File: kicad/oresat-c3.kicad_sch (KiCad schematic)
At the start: 0 parts

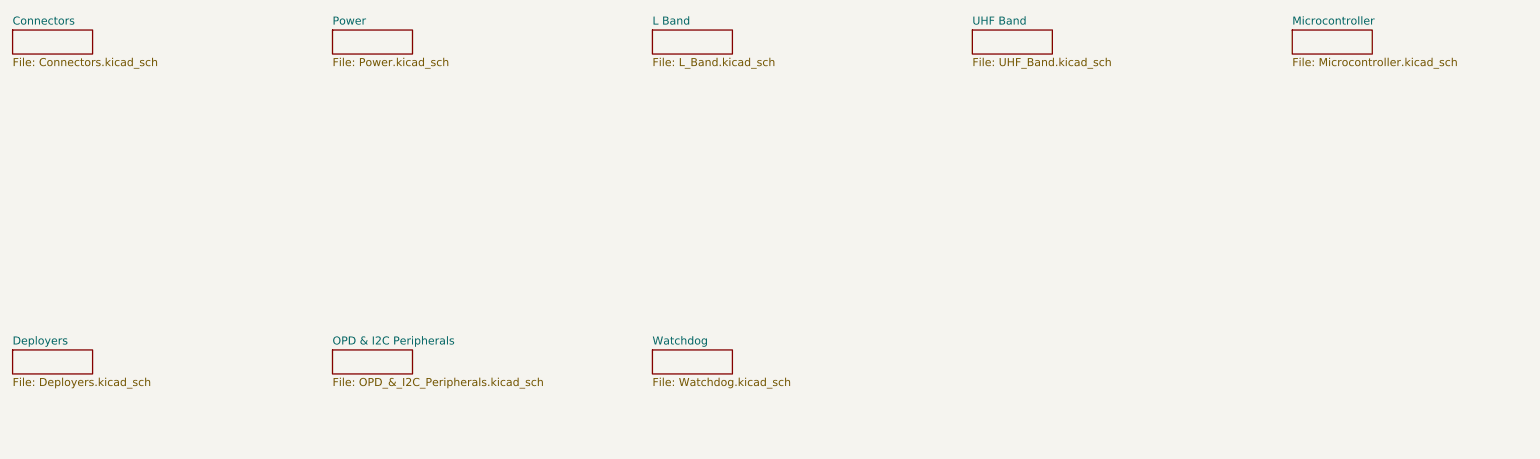
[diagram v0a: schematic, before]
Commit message: Converted kicad directory over to our latest Octavo-based v6 design starting from the GPS card.
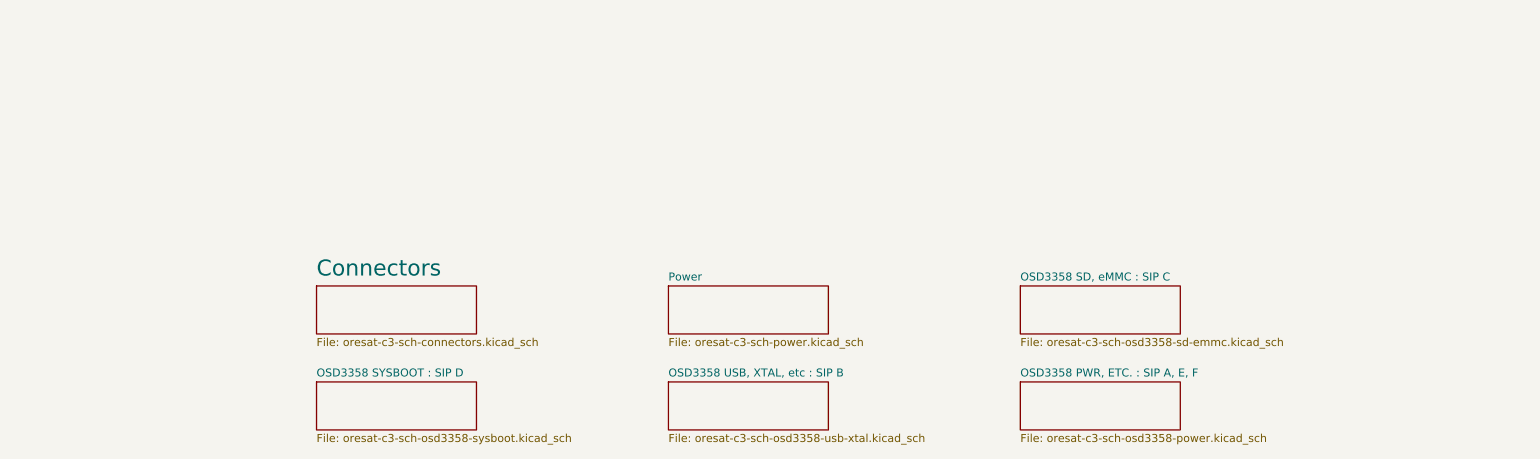
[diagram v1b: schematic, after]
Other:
- removed sheet Deployers
- removed sheet L Band
- removed sheet Microcontroller
- removed sheet OPD & I2C Peripherals
- removed sheet UHF Band
- removed sheet Watchdog
- added sheet OSD3358 PWR, ETC. : SIP A, E, F (oresat-c3-sch-osd3358-power.kicad_sch)
- added sheet OSD3358 SD, eMMC : SIP C (oresat-c3-sch-osd3358-sd-emmc.kicad_sch)
- added sheet OSD3358 SYSBOOT : SIP D (oresat-c3-sch-osd3358-sysboot.kicad_sch)
- added sheet OSD3358 USB, XTAL, etc : SIP B (oresat-c3-sch-osd3358-usb-xtal.kicad_sch)
- sheet Connectors: file Connectors.kicad_sch -> oresat-c3-sch-connectors.kicad_sch
- sheet Power: file Power.kicad_sch -> oresat-c3-sch-power.kicad_sch

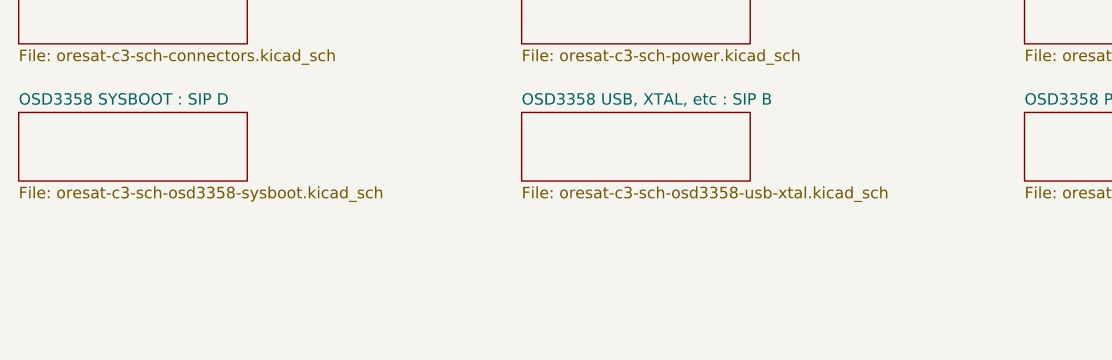
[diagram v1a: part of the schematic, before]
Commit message: Started moving RF schematic bits over to KiCad
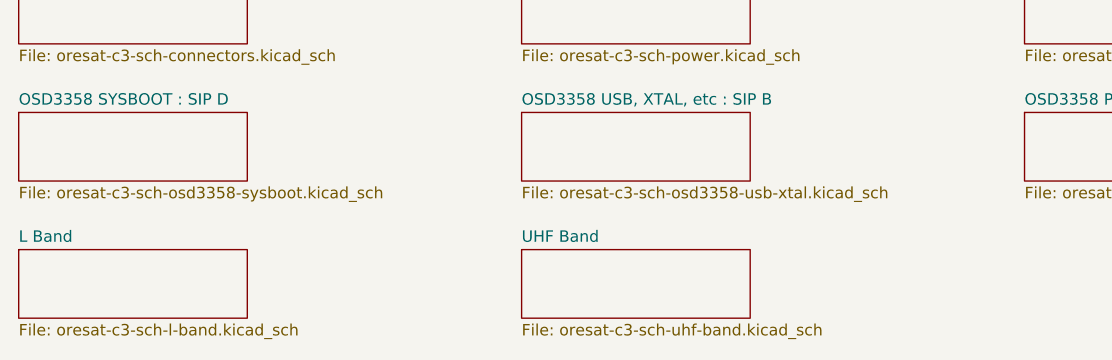
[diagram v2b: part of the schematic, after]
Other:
- added sheet L Band (oresat-c3-sch-l-band.kicad_sch)
- added sheet UHF Band (oresat-c3-sch-uhf-band.kicad_sch)
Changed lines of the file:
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@@
 (kicad_sch (version 20230121) (generator eeschema)
-  (paper "B")
+  (paper "USLedger")
+  (sheet (at 129.54 96.52) (size 25.4 7.62) (fields_autoplaced)
+    (stroke (width 0.1524) (type solid))
+    (fill (color 0 0 0 0.0000))
+    (property "Sheetname" "UHF Band" (at 129.54 95.8084 0)
+      (effects (font (size 1.27 1.27)) (justify left bottom))
+    )
+    (property "Sheetfile" "oresat-c3-sch-uhf-band.kicad_sch" (at 129.54 104.7246 0)
+      (effects (font (size 1.27 1.27)) (justify left top))
+    )
+    (instances
+      (project "oresat-c3"
+        (path "/65d12cdd-c326-4033-9053-c59fa4e0b25e" (page "9"))
+      )
+    )
+  )
   (sheet (at 185.42 81.28) (size 25.4 7.62) (fields_autoplaced)
     (stroke (width 0.1524) (type solid))
@@
       )
     )
+  )
+  (sheet (at 73.66 96.52) (size 25.4 7.62) (fields_autoplaced)
+    (stroke (width 0.1524) (type solid))
+    (fill (color 0 0 0 0.0000))
+    (property "Sheetname" "L Band" (at 73.66 95.8084 0)
+      (effects (font (size 1.27 1.27)) (justify left bottom))
+    )
+    (property "Sheetfile" "oresat-c3-sch-l-band.kicad_sch" (at 73.66 104.7246 0)
+      (effects (font (size 1.27 1.27)) (justify left top))
+    )
+    (instances
+      (project "oresat-c3"
+        (path "/65d12cdd-c326-4033-9053-c59fa4e0b25e" (page "8"))
+      )
+    )

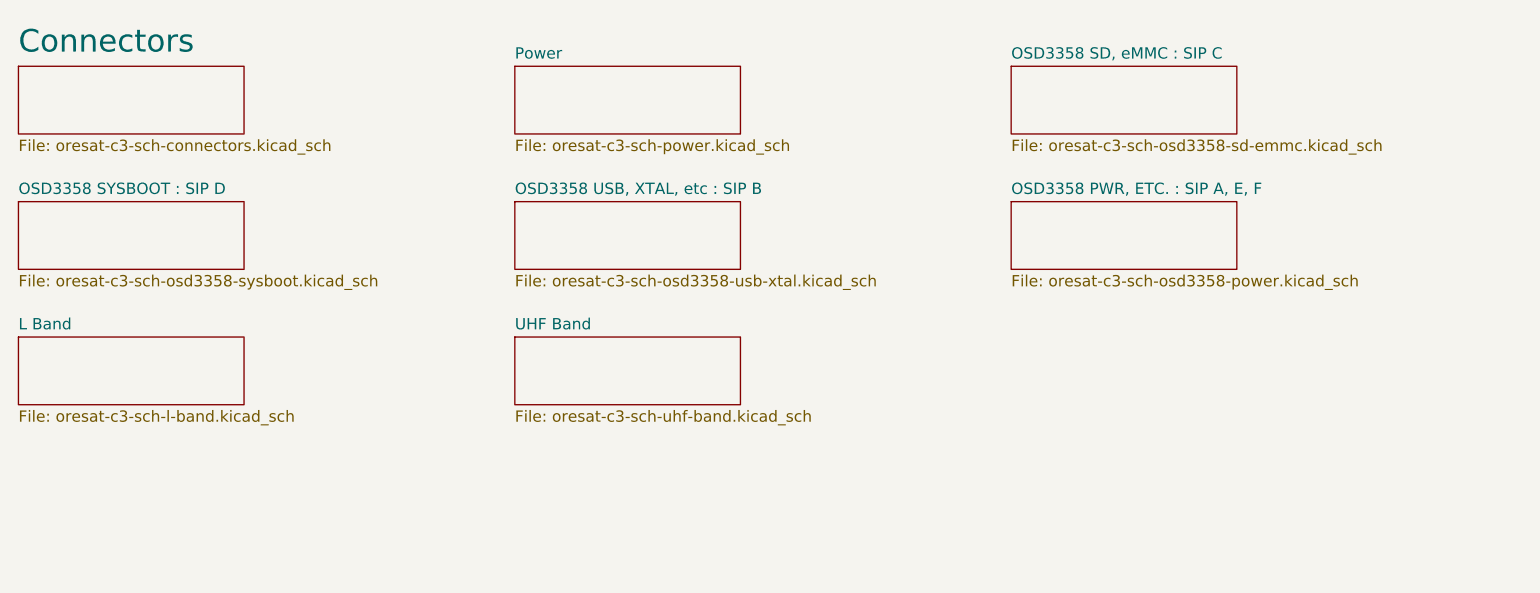
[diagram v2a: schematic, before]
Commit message: Added watchdog and I2C sheets; fixed library paths and library references. Started on watchdog schematic.
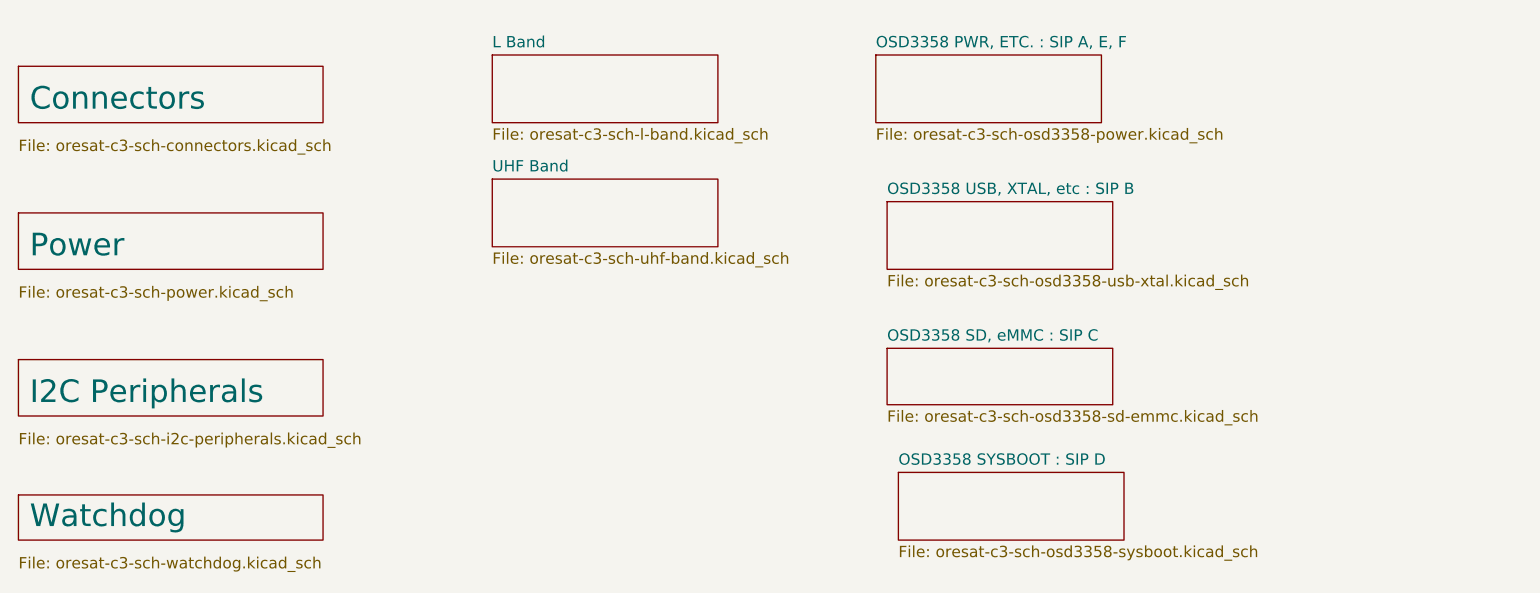
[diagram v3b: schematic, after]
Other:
- added sheet I2C Peripherals (oresat-c3-sch-i2c-peripherals.kicad_sch)
- added sheet Watchdog (oresat-c3-sch-watchdog.kicad_sch)
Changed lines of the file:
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@@
 (kicad_sch (version 20230121) (generator eeschema)
   (paper "USLedger")
-  (sheet (at 129.54 96.52) (size 25.4 7.62) (fields_autoplaced)
+  (sheet (at 127 78.74) (size 25.4 7.62) (fields_autoplaced)
     (stroke (width 0.1524) (type solid))
     (fill (color 0 0 0 0.0000))
-    (property "Sheetname" "UHF Band" (at 129.54 95.8084 0)
+    (property "Sheetname" "UHF Band" (at 127 78.0284 0)
       (effects (font (size 1.27 1.27)) (justify left bottom))
     )
-    (property "Sheetfile" "oresat-c3-sch-uhf-band.kicad_sch" (at 129.54 104.7246 0)
+    (property "Sheetfile" "oresat-c3-sch-uhf-band.kicad_sch" (at 127 86.9446 0)
       (effects (font (size 1.27 1.27)) (justify left top))
     )
@@
     )
   )
-  (sheet (at 185.42 81.28) (size 25.4 7.62) (fields_autoplaced)
+  (sheet (at 170.18 64.77) (size 25.4 7.62) (fields_autoplaced)
     (stroke (width 0.1524) (type solid))
     (fill (color 0 0 0 0.0000))
-    (property "Sheetname" "OSD3358 PWR, ETC. : SIP A, E, F" (at 185.42 80.5684 0)
+    (property "Sheetname" "OSD3358 PWR, ETC. : SIP A, E, F" (at 170.18 64.0584 0)
       (effects (font (size 1.27 1.27)) (justify left bottom))
     )
-    (property "Sheetfile" "oresat-c3-sch-osd3358-power.kicad_sch" (at 185.42 89.4846 0)
+    (property "Sheetfile" "oresat-c3-sch-osd3358-power.kicad_sch" (at 170.18 72.9746 0)
       (effects (font (size 1.27 1.27)) (justify left top))
     )
@@
     )
   )
-  (sheet (at 73.66 81.28) (size 25.4 7.62) (fields_autoplaced)
+  (sheet (at 172.72 111.76) (size 25.4 7.62) (fields_autoplaced)
     (stroke (width 0.1524) (type solid))
     (fill (color 0 0 0 0.0000))
-    (property "Sheetname" "OSD3358 SYSBOOT : SIP D" (at 73.66 80.5684 0)
+    (property "Sheetname" "OSD3358 SYSBOOT : SIP D" (at 172.72 111.0484 0)
       (effects (font (size 1.27 1.27)) (justify left bottom))
     )
-    (property "Sheetfile" "oresat-c3-sch-osd3358-sysboot.kicad_sch" (at 73.66 89.4846 0)
+    (property "Sheetfile" "oresat-c3-sch-osd3358-sysboot.kicad_sch" (at 172.72 119.9646 0)
       (effects (font (size 1.27 1.27)) (justify left top))
     )
@@
     )
   )
-  (sheet (at 129.54 81.28) (size 25.4 7.62) (fields_autoplaced)
+  (sheet (at 171.45 81.28) (size 25.4 7.62) (fields_autoplaced)
     (stroke (width 0.1524) (type solid))
     (fill (color 0 0 0 0.0000))
-    (property "Sheetname" "OSD3358 USB, XTAL, etc : SIP B" (at 129.54 80.5684 0)
+    (property "Sheetname" "OSD3358 USB, XTAL, etc : SIP B" (at 171.45 80.5684 0)
       (effects (font (size 1.27 1.27)) (justify left bottom))
     )
-    (property "Sheetfile" "oresat-c3-sch-osd3358-usb-xtal.kicad_sch" (at 129.54 89.4846 0)
+    (property "Sheetfile" "oresat-c3-sch-osd3358-usb-xtal.kicad_sch" (at 171.45 89.4846 0)
       (effects (font (size 1.27 1.27)) (justify left top))
     )
@@
     )
   )
-  (sheet (at 73.66 96.52) (size 25.4 7.62) (fields_autoplaced)
+  (sheet (at 127 64.77) (size 25.4 7.62) (fields_autoplaced)
     (stroke (width 0.1524) (type solid))
     (fill (color 0 0 0 0.0000))
-    (property "Sheetname" "L Band" (at 73.66 95.8084 0)
+    (property "Sheetname" "L Band" (at 127 64.0584 0)
       (effects (font (size 1.27 1.27)) (justify left bottom))
     )
-    (property "Sheetfile" "oresat-c3-sch-l-band.kicad_sch" (at 73.66 104.7246 0)
+    (property "Sheetfile" "oresat-c3-sch-l-band.kicad_sch" (at 127 72.9746 0)
       (effects (font (size 1.27 1.27)) (justify left top))
     )
@@
     )
   )
-  (sheet (at 129.54 66.04) (size 25.4 7.62) (fields_autoplaced)
+  (sheet (at 73.66 82.55) (size 34.29 6.35)
     (stroke (width 0.1524) (type solid))
     (fill (color 0 0 0 0.0000))
-    (property "Sheetname" "Power" (at 129.54 65.3284 0)
-      (effects (font (size 1.27 1.27)) (justify left bottom))
+    (property "Sheetname" "Power" (at 74.93 87.63 0)
+      (effects (font (size 2.54 2.54)) (justify left bottom))
     )
-    (property "Sheetfile" "oresat-c3-sch-power.kicad_sch" (at 129.54 74.2446 0)
+    (property "Sheetfile" "oresat-c3-sch-power.kicad_sch" (at 73.66 90.7546 0)
       (effects (font (size 1.27 1.27)) (justify left top))
     )
@@
     )
   )
-  (sheet (at 73.66 66.04) (size 25.4 7.62) (fields_autoplaced)
+  (sheet (at 73.66 114.3) (size 34.29 5.08)
     (stroke (width 0.1524) (type solid))
     (fill (color 0 0 0 0.0000))
-    (property "Sheetname" "Connectors" (at 73.66 64.6934 0)
+    (property "Sheetname" "Watchdog" (at 74.93 118.11 0)
+      (effects (font (size 2.54 2.54)) (justify left bottom))
+    )
+    (property "Sheetfile" "oresat-c3-sch-watchdog.kicad_sch" (at 73.66 121.2346 0)
+      (effects (font (size 1.27 1.27)) (justify left top))
+    )
+    (property "Field2" "" (at 73.66 114.3 0)
+      (effects (font (size 1.27 1.27)) hide)
+    )
+    (instances
+      (project "oresat-c3"
+        (path "/65d12cdd-c326-4033-9053-c59fa4e0b25e" (page "10"))
+      )
+    )
+  )
+  (sheet (at 73.66 99.06) (size 34.29 6.35)
+    (stroke (width 0.1524) (type solid))
+    (fill (color 0 0 0 0.0000))
+    (property "Sheetname" "I2C Peripherals" (at 74.93 104.14 0)
+      (effects (font (size 2.54 2.54)) (justify left bottom))
+    )
+    (property "Sheetfile" "oresat-c3-sch-i2c-peripherals.kicad_sch" (at 73.66 107.2646 0)
+      (effects (font (size 1.27 1.27)) (justify left top))
+    )
+    (instances
+      (project "oresat-c3"
+        (path "/65d12cdd-c326-4033-9053-c59fa4e0b25e" (page "11"))
+      )
+    )
+  )
+  (sheet (at 73.66 66.04) (size 34.29 6.35)
+    (stroke (width 0.1524) (type solid))
+    (fill (color 0 0 0 0.0000))
+    (property "Sheetname" "Connectors" (at 74.93 71.12 0)
       (effects (font (size 2.54 2.54)) (justify left bottom))
     )
@@
     )
   )
-  (sheet (at 185.42 66.04) (size 25.4 7.62) (fields_autoplaced)
+  (sheet (at 171.45 97.79) (size 25.4 6.35) (fields_autoplaced)
     (stroke (width 0.1524) (type solid))
     (fill (color 0 0 0 0.0000))
-    (property "Sheetname" "OSD3358 SD, eMMC : SIP C" (at 185.42 65.3284 0)
+    (property "Sheetname" "OSD3358 SD, eMMC : SIP C" (at 171.45 97.0784 0)
       (effects (font (size 1.27 1.27)) (justify left bottom))
     )
-    (property "Sheetfile" "oresat-c3-sch-osd3358-sd-emmc.kicad_sch" (at 185.42 74.2446 0)
+    (property "Sheetfile" "oresat-c3-sch-osd3358-sd-emmc.kicad_sch" (at 171.45 104.7246 0)
       (effects (font (size 1.27 1.27)) (justify left top))
     )

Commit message: Rough draft of watchdog and I2C system schematics.
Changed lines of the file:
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@@
 (kicad_sch (version 20230121) (generator eeschema)
   (paper "USLedger")
-  (sheet (at 127 78.74) (size 25.4 7.62) (fields_autoplaced)
+  (sheet (at 127 82.55) (size 25.4 6.35)
     (stroke (width 0.1524) (type solid))
     (fill (color 0 0 0 0.0000))
-    (property "Sheetname" "UHF Band" (at 127 78.0284 0)
-      (effects (font (size 1.27 1.27)) (justify left bottom))
+    (property "Sheetname" "UHF Band" (at 128.27 87.63 0)
+      (effects (font (size 2.54 2.54)) (justify left bottom))
     )
-    (property "Sheetfile" "oresat-c3-sch-uhf-band.kicad_sch" (at 127 86.9446 0)
+    (property "Sheetfile" "oresat-c3-sch-uhf-band.kicad_sch" (at 127 90.7546 0)
       (effects (font (size 1.27 1.27)) (justify left top))
     )
@@
     )
   )
-  (sheet (at 127 64.77) (size 25.4 7.62) (fields_autoplaced)
+  (sheet (at 127 66.04) (size 25.4 6.35)
     (stroke (width 0.1524) (type solid))
     (fill (color 0 0 0 0.0000))
-    (property "Sheetname" "L Band" (at 127 64.0584 0)
-      (effects (font (size 1.27 1.27)) (justify left bottom))
+    (property "Sheetname" "L Band" (at 128.27 71.12 0)
+      (effects (font (size 2.54 2.54)) (justify left bottom))
     )
-    (property "Sheetfile" "oresat-c3-sch-l-band.kicad_sch" (at 127 72.9746 0)
+    (property "Sheetfile" "oresat-c3-sch-l-band.kicad_sch" (at 127 74.2446 0)
       (effects (font (size 1.27 1.27)) (justify left top))
     )
